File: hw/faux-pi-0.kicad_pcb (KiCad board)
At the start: 4 copper layers, 65 x 30 mm, 67 parts, among them J1 PWR_IN, J10 USB, J2 DEBUG, J3 RUN, J6 HDMI_C_1.4, J8 GPIO, J9 Micro_SD_Card_Det, SW1 RESET, SW2 BOOTSEL, U1 RP2040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

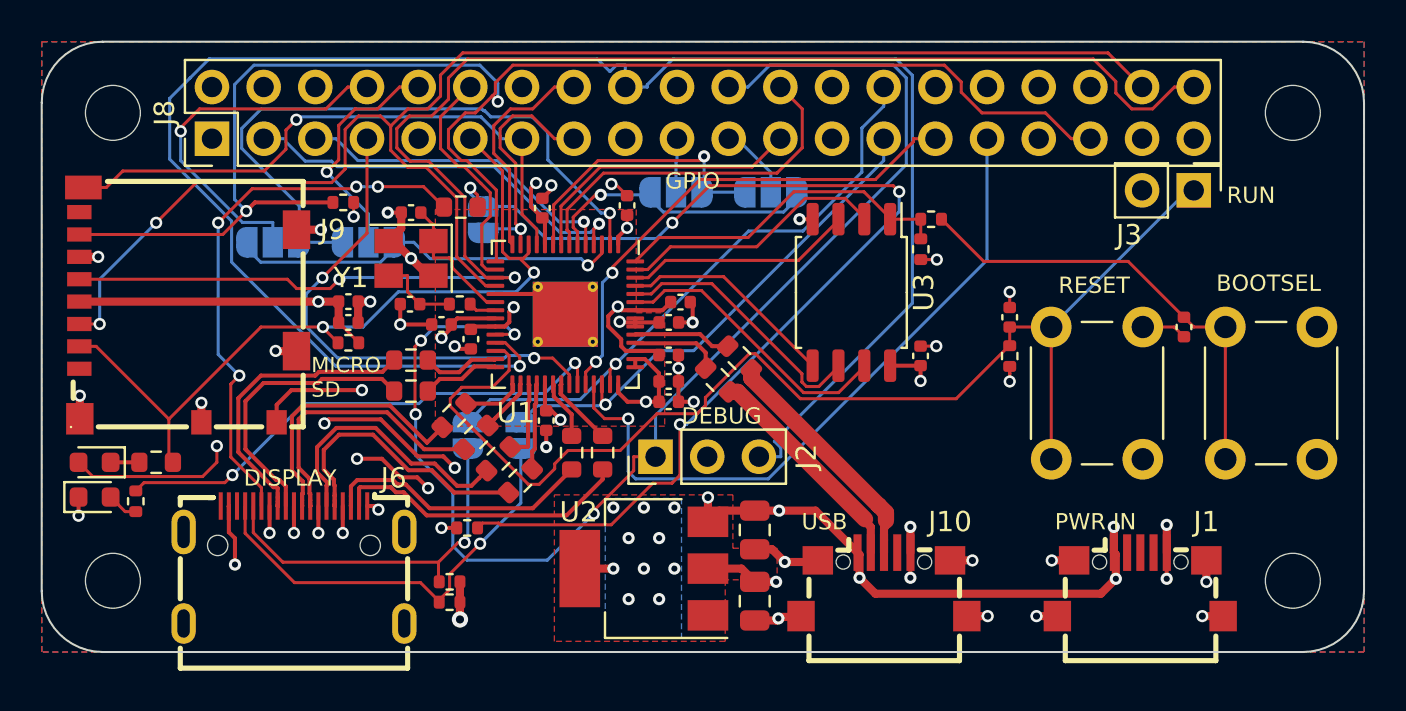
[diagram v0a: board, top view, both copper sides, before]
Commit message: Expose BOOTSEL and RUN on GPIO header
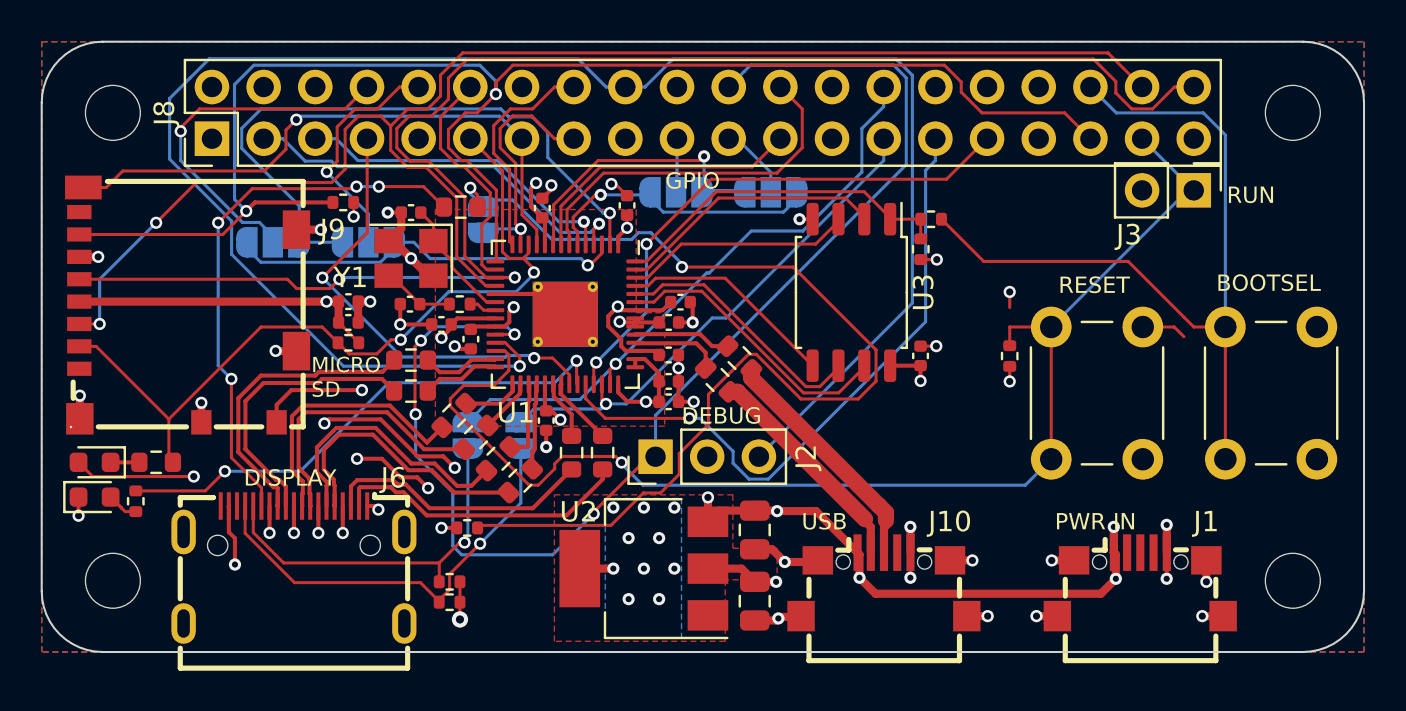
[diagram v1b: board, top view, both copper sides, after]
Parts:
- removed C3, C6: 100n, Capacitor_SMD:C_0402_1005Metric
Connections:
- J8 pad 36: unconnected-(J8-Pad36) -> /BOOTSEL
- J8 pad 37: unconnected-(J8-Pad37) -> /RUN
- R20 pad 1: Net-(C6-Pad1) -> /BOOTSEL
- SW2 pad 2: Net-(C6-Pad1) -> /BOOTSEL
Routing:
- net /BOOTSEL: track 0.00 -> 39.7 mm
- net Net-(C6-Pad1): track 22.6 -> 0.00 mm
- net /PICO_ADC1: track 33.9 -> 26.9 mm, vias 1 -> 2
- net /PICO_ADC0: track 24.9 -> 31.8 mm, vias 2 -> 1
- net +3V3: track 52.6 -> 50.0 mm
- net /PICO_PWM: track 25.0 -> 22.4 mm
- net /RUN: track 58.7 -> 61.2 mm, vias 0 -> 1
- net /PICO_SWD: track 90.1 -> 88.0 mm
- net /DVI_CEC: track 54.3 -> 52.7 mm, vias 4 -> 2
- net Net-(J6-Pad14): track 27.9 -> 27.1 mm
- net /PICO_SPI1_RX: track 77.2 -> 76.4 mm
- net /PICO_SWCLK: track 63.0 -> 62.3 mm

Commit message: docs & remove UART jumpers
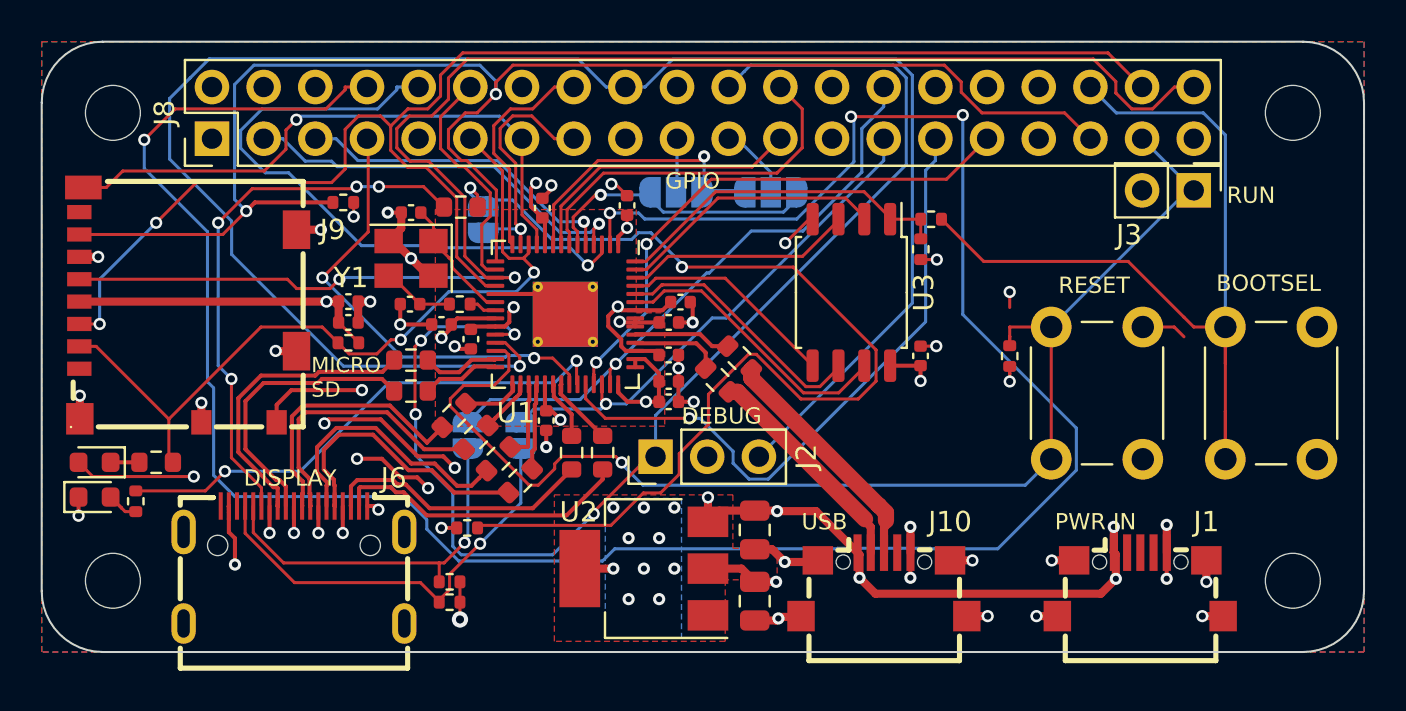
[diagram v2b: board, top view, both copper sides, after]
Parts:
- removed JP2, JP4: SolderJumper_3_Open, Jumper:SolderJumper-3_P1.3mm_Open_RoundedPad1.0x1.5mm
- JP1: value SolderJumper_3_Open -> SPI0_PICO
- JP3: value SolderJumper_3_Open -> SPI0_POCI
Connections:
- J8 pad 10: /RX -> /PICO_UART0_RX
- J8 pad 8: /TX -> /PICO_UART0_TX
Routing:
- net /PICO_UART0_TX: track 31.7 -> 118.7 mm, vias 1 -> 4
- net /TX: track 18.0 -> 0.00 mm, vias 1 -> 0
- net /PICO_UART0_RX: track 19.8 -> 31.6 mm
- net /RX: track 11.5 -> 0.00 mm, vias 1 -> 0
- net /BOOTSEL: track 39.7 -> 43.8 mm
- net GND: track 72.2 -> 73.3 mm
- net +3V3: track 50.0 -> 50.9 mm
- net /DVI_SCL: track 18.3 -> 19.0 mm
- net /PICO_I2C1_SCL: track 16.0 -> 16.6 mm
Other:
- board text added: "C"
- board text added: "CEC"
- board text added: "DANGER!"
- board text added: "DVI 5V!"
- board text added: "P"
- board text added: "SCL"
- board text added: "SDA"
- board text added: "SPI0"
- board text added: "https://github.com/dlehenbauer/faux-pi-zero"

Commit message: tweaks
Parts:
- renumbered JP3 to JP2, JP7 to JP3, JP8 to JP4, JP9 to JP5
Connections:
- net /MISO0 renamed /SPI0_POCI0
- net /MOSI0 renamed /SPI0_PICO0
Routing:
- net /PICO_UART0_TX: track 118.7 -> 35.8 mm, vias 4 -> 2
- net /PICO_SWD: track 88.0 -> 85.6 mm
- net /PICO_PWM: track 22.7 -> 21.3 mm
- net GND: track 73.3 -> 72.1 mm, vias 42 -> 41
- net +3V3: track 50.9 -> 51.9 mm
- net /SD_~{CS}: track 39.4 -> 38.8 mm
- net /PICO_SPI1_SCLK: track 75.9 -> 75.2 mm
- net /PICO_ADC0: track 32.2 -> 32.8 mm
- net /PICO_ADC1: track 27.3 -> 27.6 mm, vias 2 -> 0
- net /PICO_SWCLK: track 62.3 -> 62.2 mm, vias 4 -> 3
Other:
- board text added: "DANGER 5V!"
- board text added: "DVI"
- board text removed: "DANGER!"
- board text removed: "DVI 5V!"
